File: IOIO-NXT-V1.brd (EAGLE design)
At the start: 100 x 80 mm, 14 parts

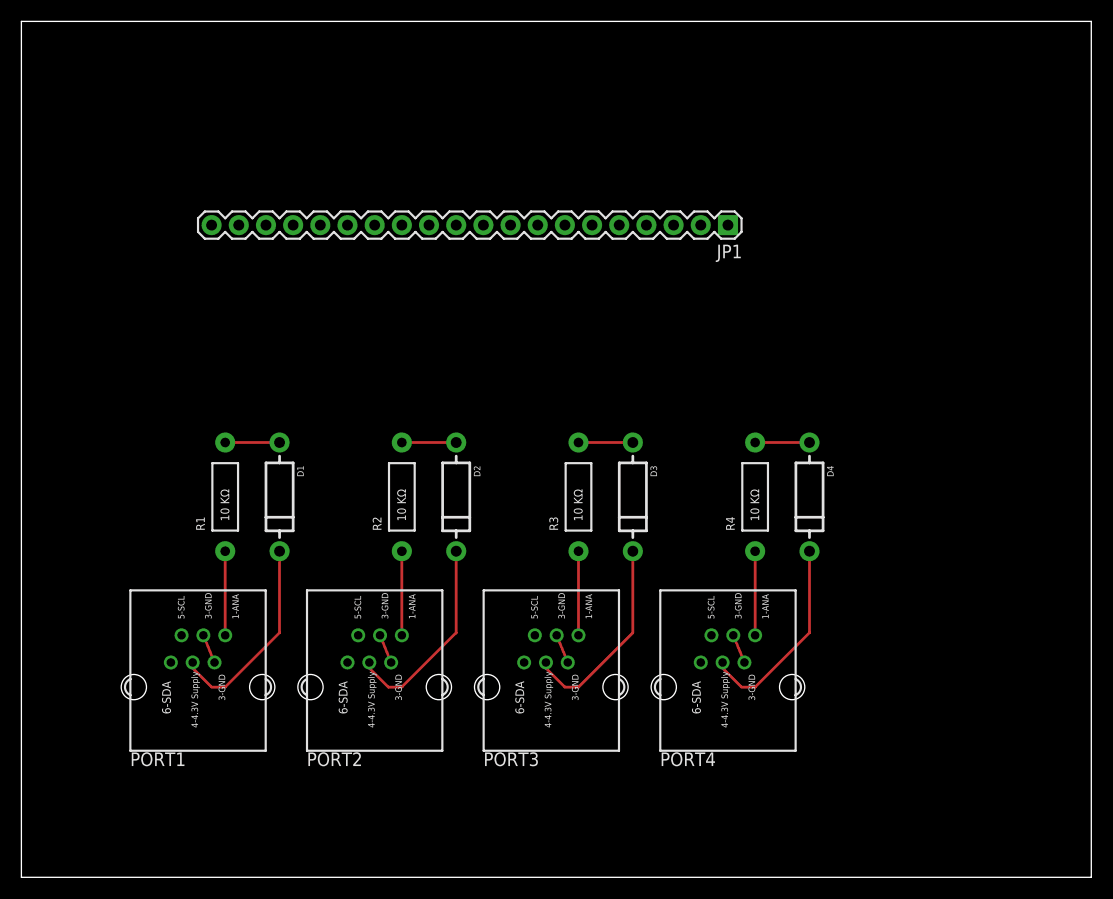
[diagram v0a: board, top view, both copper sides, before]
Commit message: Added IOIO headers and EA logo.  Waiting for analog pin #s
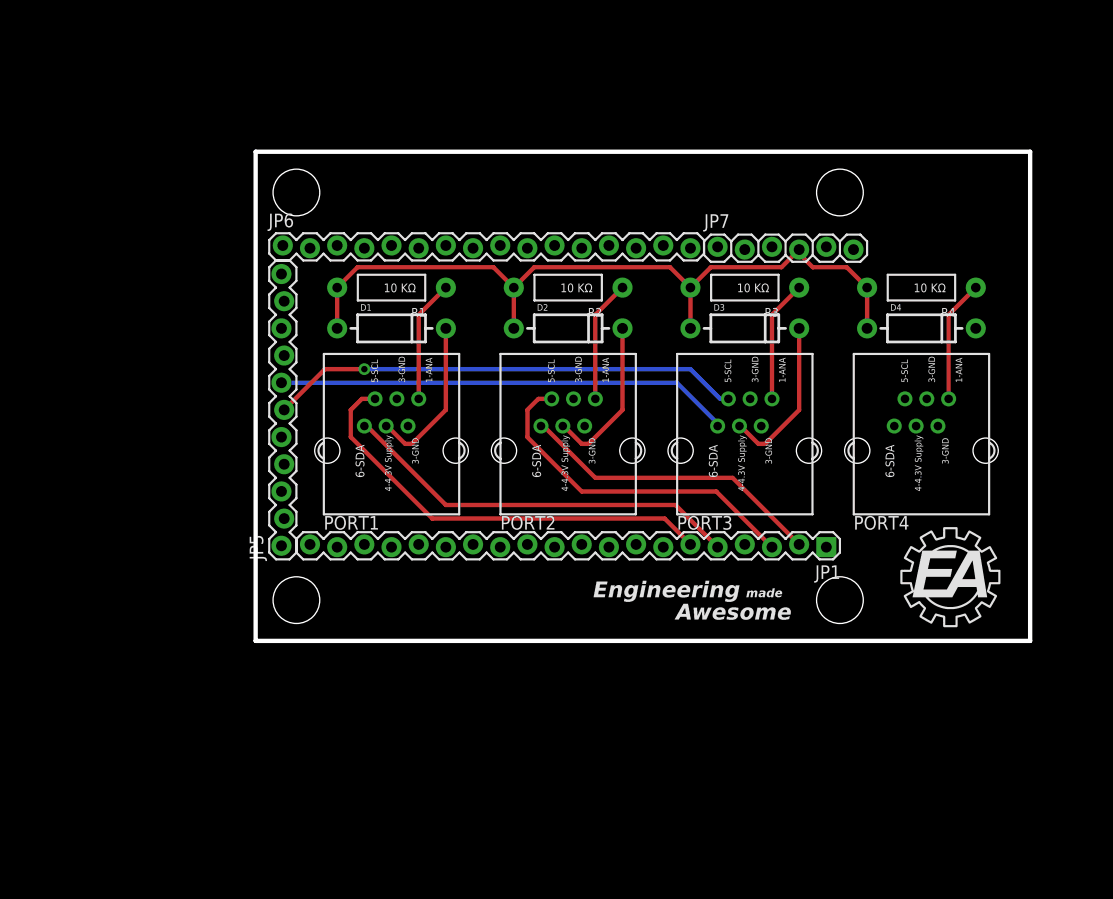
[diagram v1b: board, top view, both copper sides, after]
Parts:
- added JP5: M11LOCK, SparkFun-Connectors:1X11_LOCK
- added JP6: M16LOCK, SparkFun-Connectors:1X16_LOCK
- added JP7: (no value), SparkFun-Connectors:1X06_LOCK
- JP1: value M20 -> M20LOCK; device SparkFun-Connectors:1X20 -> SparkFun-Connectors:1X20_LOCK
- moved FRAME1 126.2 mm to (46.0, 11.9)
- moved JP1 31.4 mm to (75.2, 31.0)
- moved PORT3 28.6 mm to (67.6, 39.9)
- moved PORT1 28.6 mm to (34.6, 39.9)
- moved PORT2 28.6 mm to (51.1, 39.9)
- moved PORT4 28.6 mm to (84.1, 39.9)
- moved R1 25.0 mm to (34.6, 55.1), turned to 180 degrees
- moved R3 25.0 mm to (67.6, 55.1), turned to 180 degrees
- moved R2 25.0 mm to (51.1, 55.1), turned to 180 degrees
- moved R4 25.0 mm to (84.1, 55.1), turned to 180 degrees
- moved D3 18.9 mm to (67.6, 51.3), turned to 0 degrees
- moved D1 18.9 mm to (34.6, 51.3), turned to 0 degrees
- moved D2 18.9 mm to (51.1, 51.3), turned to 0 degrees
- moved D4 18.9 mm to (84.1, 51.3), turned to 0 degrees
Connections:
- new net P10: JP1.11
- new net P11: JP1.12
- new net P12: JP1.13
- new net P13: JP1.14
- new net P14: JP1.15
- new net P15: JP1.16
- new net P16: JP1.17
- new net P17: JP1.18
- new net P18: JP1.19
- new net P19: JP1.20
- new net P20: JP5.1
- new net P21: JP5.2
- new net P22: JP5.3
- new net P23: JP5.4
- new net P24: JP5.5
- new net P27: JP5.8
- new net P28: JP5.9
- new net P29: JP5.10
- new net P3: JP1.4
- new net P30: JP5.11
- new net P31: JP6.1
- new net P32: JP6.2
- new net P33: JP6.3
- new net P34: JP6.4
- new net P35: JP6.5
- new net P36: JP6.6
- new net P37: JP6.7
- new net P38: JP6.8
- new net P39: JP6.9
- new net P40: JP6.10
- new net P41: JP6.11
- new net P42: JP6.12
- new net P43: JP6.13
- new net P44: JP6.14
- new net P45: JP6.15
- new net P46: JP6.16
- new net P6: JP1.7
- new net P7: JP1.8
- new net P8: JP1.9
- new net P9: JP1.10
- new net V3.3: JP7.2
- new net VIN: JP7.6
- net GND: now also JP7.1, JP7.3, JP7.5
- net SCL1: now also JP1.6; no longer JP1.5
- net SCL2: now also JP1.3
- net SCL3: now also JP5.6
- net SDA1: now also JP1.5; no longer JP1.4
- net SDA2: now also JP1.2; no longer JP1.16
- net SDA3: now also JP5.7; no longer JP1.17
- net SDA4: no longer JP1.18
- net VCC: now also JP7.4
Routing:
- net VCC: track 20.3 -> 71.1 mm
- net SCL3: track 0.00 -> 44.2 mm, vias 0 -> 1
- net SDA3: track 0.00 -> 42.6 mm
- net SCL1: track 0.00 -> 41.1 mm
- net SDA1: track 0.00 -> 37.7 mm
- net SCL2: track 0.00 -> 32.4 mm
- net SDA2: track 0.00 -> 28.7 mm
- net N$2: track 19.1 -> 0.00 mm
- net GND: track 11.0 -> 0.00 mm
- net N$1: track 19.1 -> 15.2 mm
- net N$4: track 19.1 -> 15.2 mm
- net N$3: track 19.1 -> 15.2 mm
- net IOIOAI4: track 7.86 -> 11.5 mm
- net IOIOAI3: track 7.86 -> 11.5 mm
- net IOIOAI2: track 7.86 -> 11.5 mm
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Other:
- board size 100 x 80 mm -> 72.4 x 45.7 mm
